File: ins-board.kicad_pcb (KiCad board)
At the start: 4 copper layers, 50 x 23 mm, 93 parts, among them P1 POWER, Q1 FDN306P, Q2 FDC638APZ, U1 24LC128, U10 HMC5883L, U11 H3LIS331DL, U2 STM32F415RGT6, U3 LTC4412, U4 MAX3051, U5 LT1965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

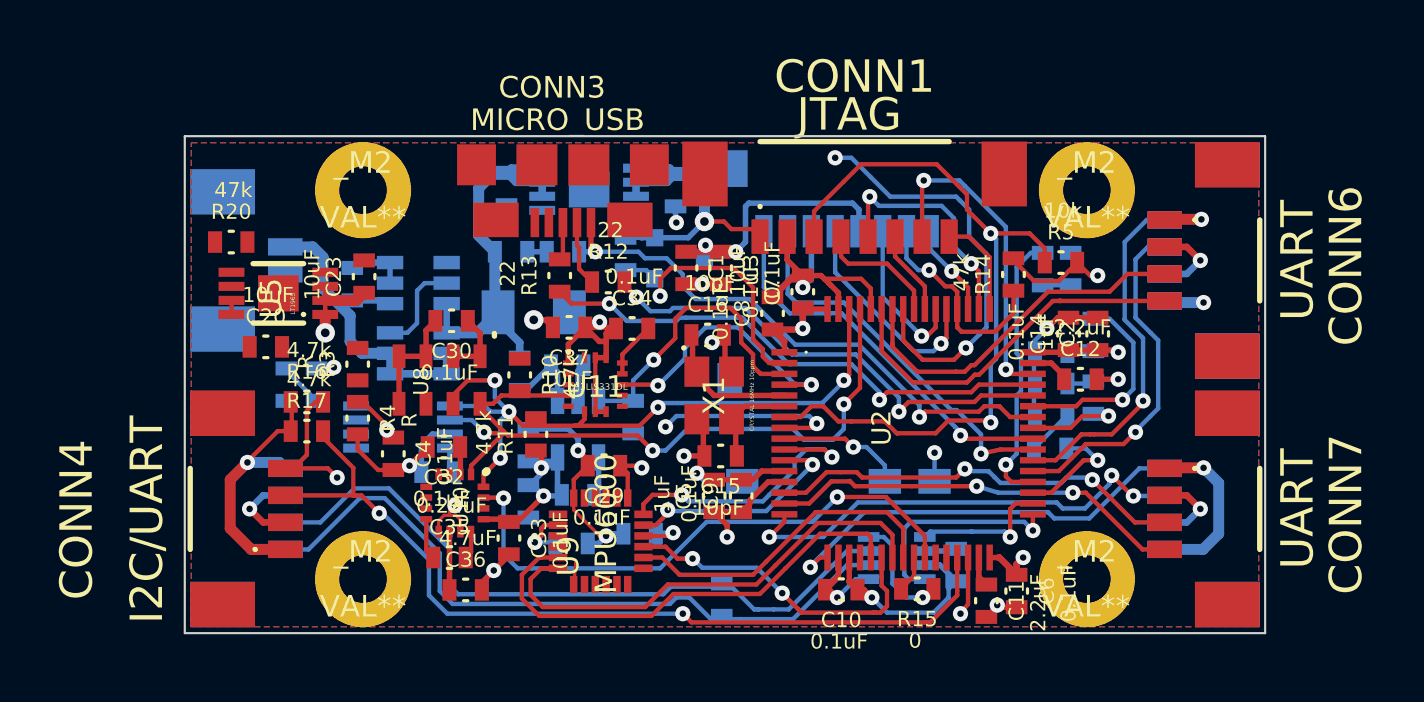
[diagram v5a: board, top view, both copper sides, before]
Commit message: power supply solder pad connector
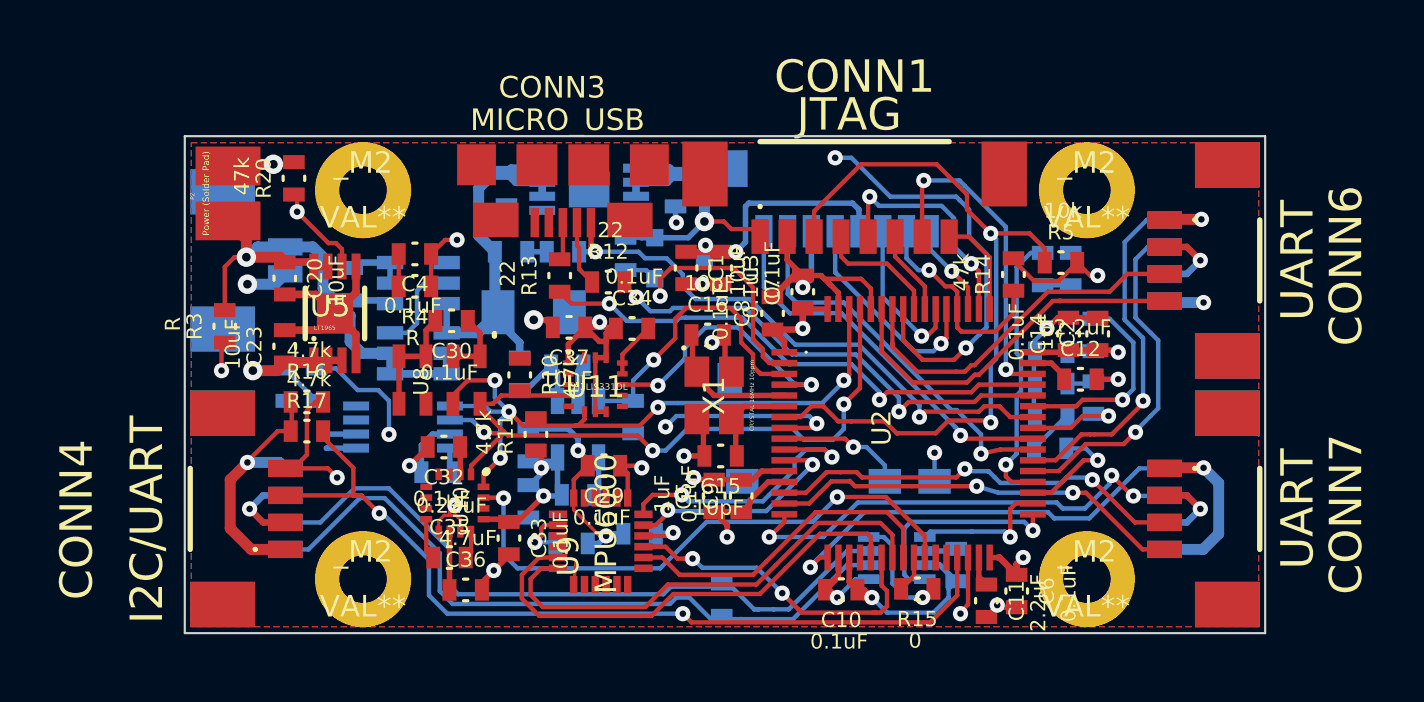
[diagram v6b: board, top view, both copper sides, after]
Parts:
- added P2: Power (Solder Pad), _Solder_Pad2.54_2, F.Cu at (34.0, 28.6)
- moved C4 9.30 mm to (42.6, 31.4), turned to 180 degrees
- moved R4 6.65 mm to (42.6, 33.0), turned to 180 degrees
- moved R3 6.39 mm to (33.9, 34.8)
- moved C23 4.89 mm to (36.6, 35.7)
- moved R20 4.14 mm to (37.0, 27.9), turned to 90 degrees
- moved C20 3.29 mm to (36.6, 32.6), turned to 270 degrees
- moved U5 2.19 mm to (38.0, 36.4), turned to 0 degrees
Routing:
- net /V_BAT_MON_AD: track 39.0 -> 56.8 mm, vias 3 -> 4
- net GND: track 92.6 -> 109.8 mm, vias 19 -> 22
- net /V_DC: track 15.4 -> 25.9 mm, vias 0 -> 1
- net VCC: track 75.1 -> 81.8 mm
- net /IO_EN: track 46.9 -> 51.6 mm, vias 2 -> 3
- net /VCC_IO: track 95.1 -> 96.5 mm
- net (no net): track 0.94 -> 0.00 mm, vias 1 -> 0

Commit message: routing 100%
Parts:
- R11: moved to B.Cu
- moved R11 3.47 mm to (45.8, 42.2)
- moved R21 3.46 mm to (54.9, 36.2), turned to 180 degrees
- moved R4 2.94 mm to (45.4, 31.9), turned to 0 degrees
- moved R10 0.50 mm to (48.0, 37.0)
- moved C33 0.21 mm to (47.0, 44.8)
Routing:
- net GND: track 109.8 -> 127.5 mm, vias 22 -> 23
- net /Sensors/VCC_A: track 30.1 -> 39.2 mm, vias 4 -> 5
- net /Sensors/I2C_SDA: track 32.1 -> 33.6 mm
- net /V_DC: track 25.9 -> 26.9 mm
- net /Sensors/H3LIS331DL_INT1: track 12.5 -> 13.2 mm

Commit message: optimize routing
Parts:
- moved R11 1.50 mm to (45.7, 43.7)
- moved D6 0.45 mm to (47.1, 30.9)
- moved F1 0.45 mm to (49.5, 30.9)
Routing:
- net GND: track 127.5 -> 133.2 mm, vias 23 -> 24
- net /Sensors/VCC_A: track 39.2 -> 42.7 mm
- added copper zone on Inner2.Cu, net GND
